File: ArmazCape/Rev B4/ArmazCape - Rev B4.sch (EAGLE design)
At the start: 167 parts, among them IC1 AT93C46EN-SH-BSOIC8, P1 RB1-125BAG1A, Q1 32.768kHz, 12.5pF, Q4 IRLML6344TRPBF, Q5 IRLML6344TRPBF, U1 L7985A, U2 L7985A, U3 DS1307ZN+, U4 24AA256-I/SN, U5 CD4050BD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

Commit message: ArmazCape - Rev B4: Reorganized schematics layout
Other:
- note added: "Mounting pads"

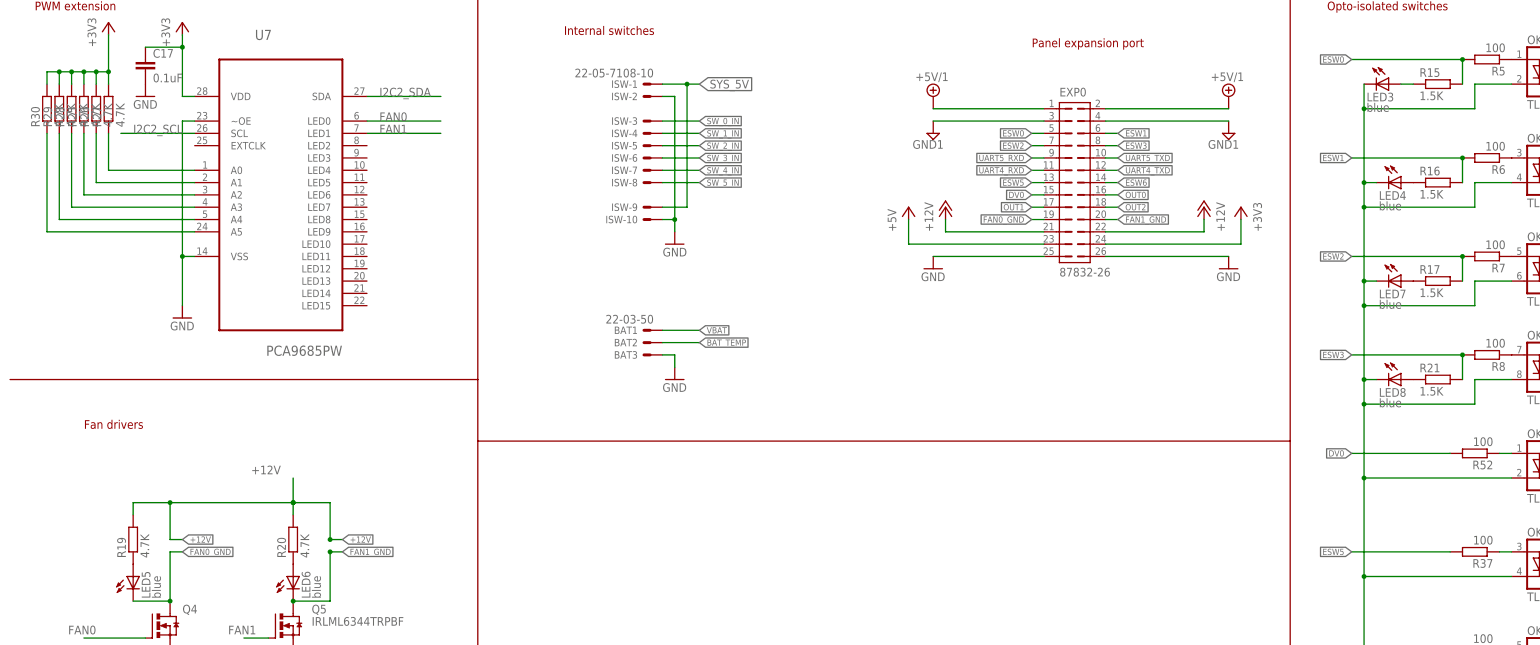
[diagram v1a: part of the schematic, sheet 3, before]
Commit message: Update attributes in ArmazCape - Rev B4
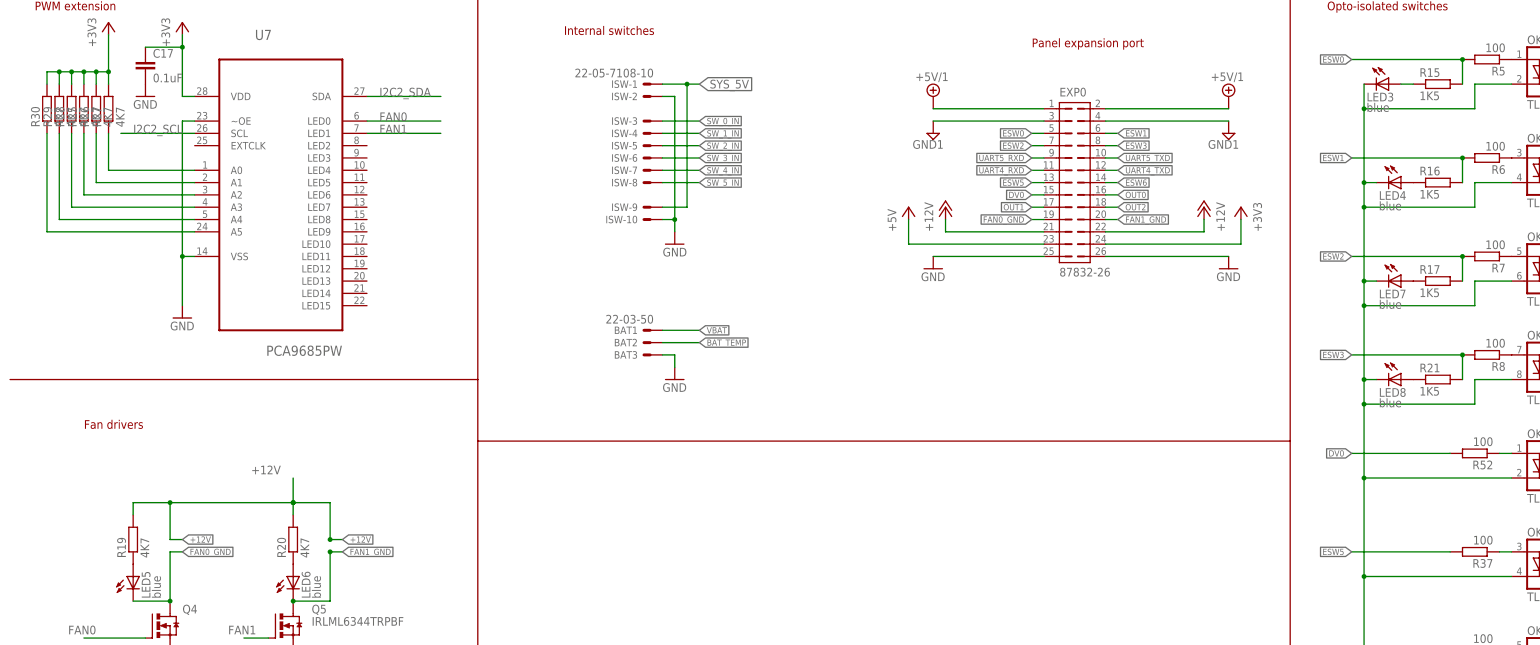
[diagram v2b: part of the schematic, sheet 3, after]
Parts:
- -25.000MHZMAAJ-T1: MF (none) -> TXC; OC_FARNELL (none) -> 1842189
- C25, C29: MPN MC0603B103K160CT -> MC0603B104K250CT; OC_FARNELL 1759003 -> 1759037
- C41: MF (none) -> MULTICOMP; MPN MC0603B104K160CT -> MC0603B104K250CT; OC_FARNELL (none) -> 1759037
- C42, C43: MF (none) -> MULTICOMP; MPN MC0603N180J500CT -> MC0603B183K160CT; OC_FARNELL (none) -> 1759006
- C9: MF MURATA -> MULTICOMP; MPN GRM1885C1H331JA01D -> MC0603B331K500CT; OC_FARNELL 8819890 -> 1759075
- GND, P1, U$7, WP: OC_FARNELL (none) -> unknown
- IC1: MF (none) -> ATMEL; OC_FARNELL (none) -> 2345627
- Q4, Q5: MF INTERNATIONAL RECTIFIER -> INFINEON
- R11: device rcl:R-EU_R0402 -> rcl:R-EU_R0603; MPN MCMR04X1600FTL -> MCWR06X1600FTL; OC_FARNELL 2072668 -> 2447260
- R13, R18, R31: value 4K7, 1% -> 4K7
- R15, R16, R17, R21: value 1.5K -> 1K5
- R19, R20, R22, R25, R26, R27, R28, R29, R30, R401, R402, R41: value 4.7K -> 4K7
- R33: MPN MCMR04X6980FTL -> MC0063W06031698R; OC_FARNELL 2073217 -> 1170773
- R68: MF (none) -> MULTICOMP; MPN MC0063W060313K01 -> MCMR06X3001FTL; OC_FARNELL (none) -> 2073461
- R73, R74: MF Multicomp Passives -> MULTICOMP; MPN MC0063W06031220R -> MCMR06X2200FTL; OC_FARNELL (none) -> 2073428
- R75: MF Multicomp Passives -> MULTICOMP; MPN MC0603WG00000T5E-TC -> MCMR06X000 PTL; OC_FARNELL (none) -> 2073345
- R76: value 4.7K -> 4K7; MF Multicomp Passives -> MULTICOMP; MPN MC0063W060314K7 -> MCMR06X4701FTL; OC_FARNELL (none) -> 2073509
- U$4: MF (none) -> MICREL SEMICONDUCTOR; MPN KSZ8851SNLI-TR -> KSZ8851SNLI TR; OC_FARNELL (none) -> 1961911

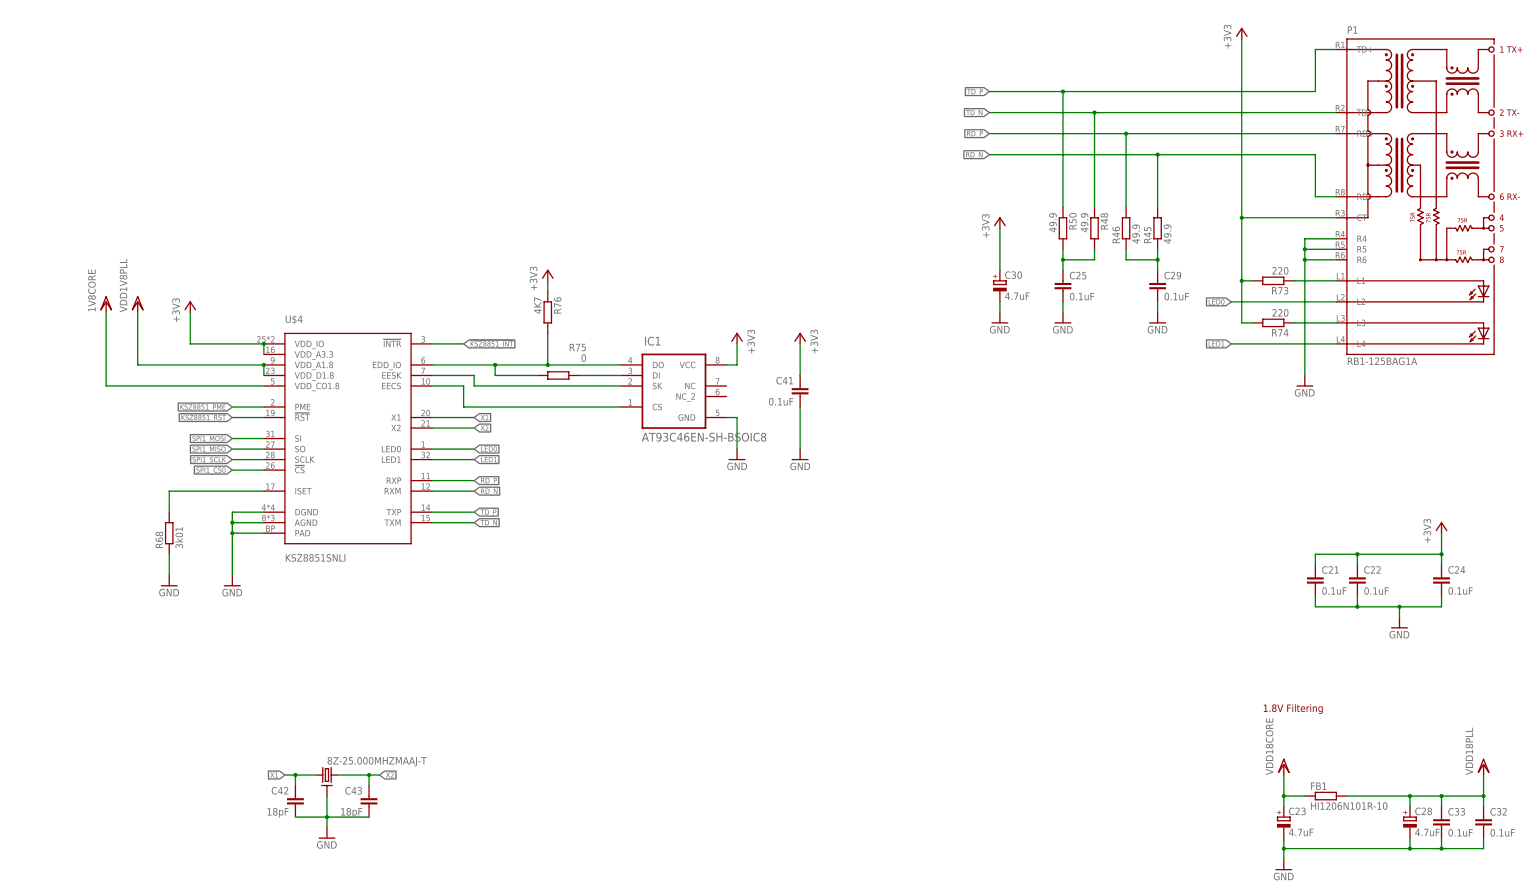
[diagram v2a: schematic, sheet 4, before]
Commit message: Reroute UART isolation
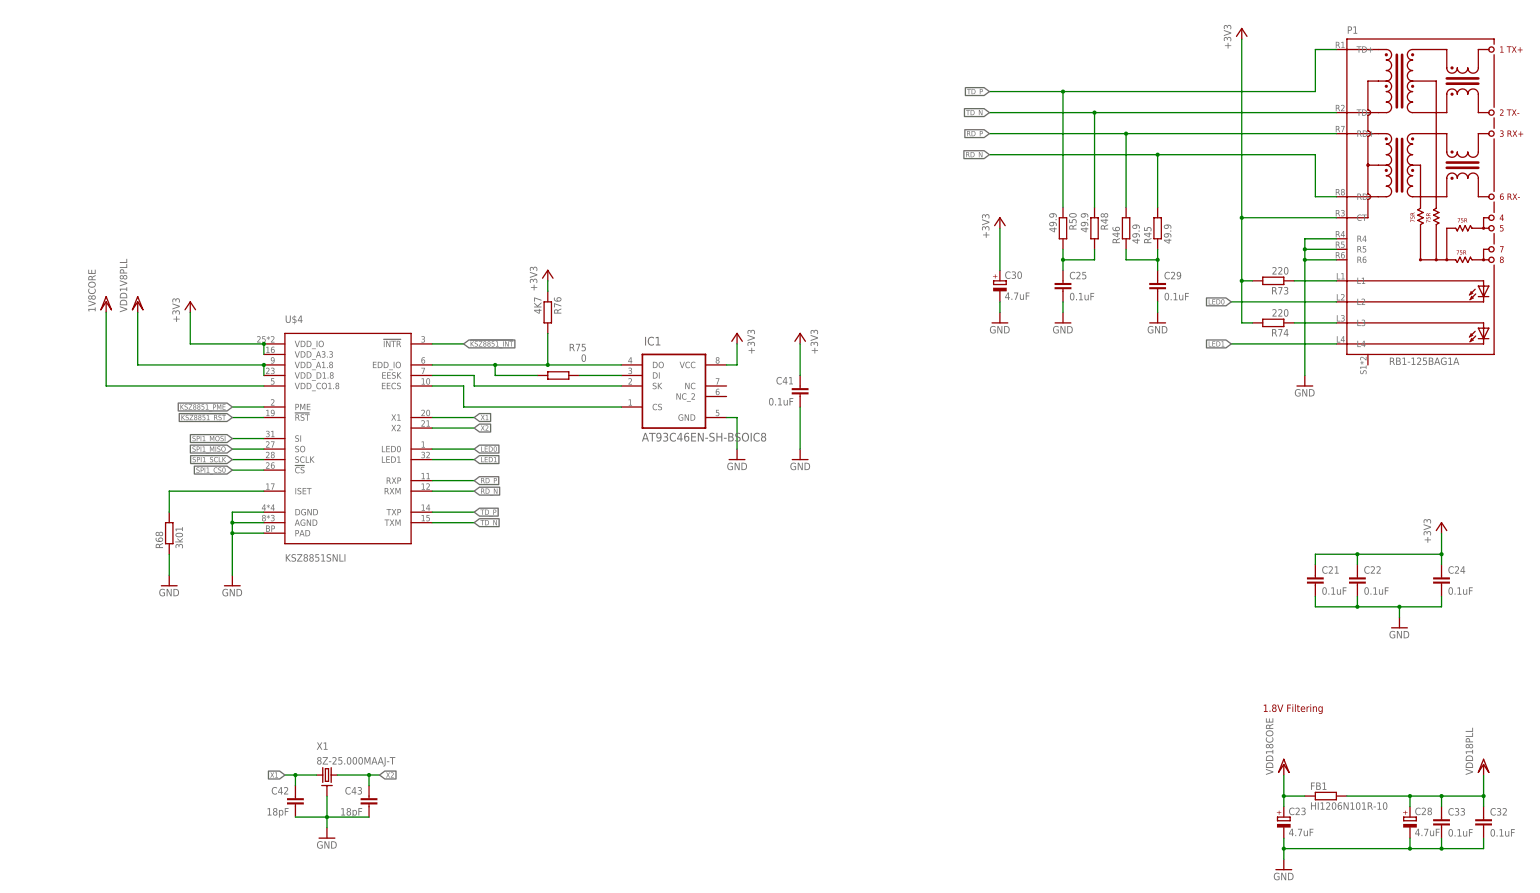
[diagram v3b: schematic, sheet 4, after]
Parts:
- X1: value 8Z-25.000MHZMAAJ-T -> 8Z-25.000MAAJ-T
- renumbered -25.000MHZMAAJ-T1 to X1
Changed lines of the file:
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@@
 <?xml version="1.0" encoding="utf-8"?>
 <!DOCTYPE eagle SYSTEM "eagle.dtd">
-<eagle version="7.6.0">
+<eagle version="7.7.0">
 <drawing>
 <settings>
@@
 <grid distance="0.1" unitdist="inch" unit="inch" style="lines" multiple="1" display="no" altdistance="0.01" altunitdist="inch" altunit="inch"/>
 <layers>
-<layer number="1" name="Top" color="16" fill="1" visible="yes" active="no"/>
-<layer number="2" name="Route2" color="17" fill="1" visible="yes" active="no"/>
-<layer number="3" name="Route3" color="4" fill="3" visible="yes" active="no"/>
-<layer number="14" name="Route14" color="1" fill="6" visible="yes" active="no"/>
-<layer number="15" name="Route15" color="19" fill="1" visible="yes" active="no"/>
-<layer number="16" name="Bottom" color="21" fill="1" visible="yes" active="no"/>
-<layer number="17" name="Pads" color="18" fill="1" visible="yes" active="no"/>
-<layer number="18" name="Vias" color="38" fill="1" visible="yes" active="no"/>
-<layer number="19" name="Unrouted" color="6" fill="1" visible="yes" active="no"/>
-<layer number="20" name="Dimension" color="7" fill="1" visible="yes" active="no"/>
-<layer number="21" name="tPlace" color="55" fill="1" visible="yes" active="no"/>
-<layer number="22" name="bPlace" color="54" fill="1" visible="yes" active="no"/>
-<layer number="23" name="tOrigins" color="15" fill="1" visible="yes" active="no"/>
-<layer number="24" name="bOrigins" color="15" fill="1" visible="yes" active="no"/>
-<layer number="25" name="tNames" color="55" fill="1" visible="yes" active="no"/>
-<layer number="26" name="bNames" color="54" fill="1" visible="yes" active="no"/>
-<layer number="27" name="tValues" color="53" fill="1" visible="yes" active="no"/>
-<layer number="28" name="bValues" color="52" fill="1" visible="yes" active="no"/>
+<layer number="1" name="Top" color="16" fill="1" visible="no" active="no"/>
+<layer number="2" name="Route2" color="17" fill="1" visible="no" active="no"/>
+<layer number="3" name="Route3" color="4" fill="3" visible="no" active="no"/>
+<layer number="14" name="Route14" color="1" fill="6" visible="no" active="no"/>
+<layer number="15" name="Route15" color="19" fill="1" visible="no" active="no"/>
+<layer number="16" name="Bottom" color="21" fill="1" visible="no" active="no"/>
+<layer number="17" name="Pads" color="18" fill="1" visible="no" active="no"/>
+<layer number="18" name="Vias" color="38" fill="1" visible="no" active="no"/>
+<layer number="19" name="Unrouted" color="6" fill="1" visible="no" active="no"/>
+<layer number="20" name="Dimension" color="7" fill="1" visible="no" active="no"/>
+<layer number="21" name="tPlace" color="55" fill="1" visible="no" active="no"/>
+<layer number="22" name="bPlace" color="54" fill="1" visible="no" active="no"/>
+<layer number="23" name="tOrigins" color="15" fill="1" visible="no" active="no"/>
+<layer number="24" name="bOrigins" color="15" fill="1" visible="no" active="no"/>
+<layer number="25" name="tNames" color="55" fill="1" visible="no" active="no"/>
+<layer number="26" name="bNames" color="54" fill="1" visible="no" active="no"/>
+<layer number="27" name="tValues" color="53" fill="1" visible="no" active="no"/>
+<layer number="28" name="bValues" color="52" fill="1" visible="no" active="no"/>
 <layer number="29" name="tStop" color="7" fill="3" visible="no" active="no"/>
 <layer number="30" name="bStop" color="7" fill="6" visible="no" active="no"/>
@@
 <layer number="35" name="tGlue" color="7" fill="4" visible="no" active="no"/>
 <layer number="36" name="bGlue" color="7" fill="5" visible="no" active="no"/>
-<layer number="37" name="tTest" color="7" fill="1" visible="yes" active="no"/>
-<layer number="38" name="bTest" color="7" fill="1" visible="yes" active="no"/>
+<layer number="37" name="tTest" color="7" fill="1" visible="no" active="no"/>
+<layer number="38" name="bTest" color="7" fill="1" visible="no" active="no"/>
 <layer number="39" name="tKeepout" color="4" fill="11" visible="no" active="no"/>
 <layer number="40" name="bKeepout" color="3" fill="11" visible="no" active="no"/>
@@
 <layer number="44" name="Drills" color="16" fill="1" visible="no" active="no"/>
 <layer number="45" name="Holes" color="35" fill="1" visible="no" active="no"/>
-<layer number="46" name="Milling" color="35" fill="1" visible="yes" active="no"/>
-<layer number="47" name="Measures" color="21" fill="1" visible="yes" active="no"/>
-<layer number="48" name="Document" color="24" fill="1" visible="yes" active="no"/>
-<layer number="49" name="Reference" color="48" fill="1" visible="yes" active="no"/>
-<layer number="50" name="dxf" color="7" fill="1" visible="yes" active="no"/>
-<layer number="51" name="tDocu" color="55" fill="1" visible="yes" active="no"/>
-<layer number="52" name="bDocu" color="54" fill="1" visible="yes" active="no"/>
-<layer number="53" name="tGND_GNDA" color="7" fill="1" visible="yes" active="no"/>
-<layer number="54" name="bGND_GNDA" color="7" fill="1" visible="yes" active="no"/>
-<layer number="56" name="wert" color="7" fill="1" visible="yes" active="no"/>
+<layer number="46" name="Milling" color="35" fill="1" visible="no" active="no"/>
+<layer number="47" name="Measures" color="21" fill="1" visible="no" active="no"/>
+<layer number="48" name="Document" color="24" fill="1" visible="no" active="no"/>
+<layer number="49" name="Reference" color="48" fill="1" visible="no" active="no"/>
+<layer number="50" name="dxf" color="7" fill="1" visible="no" active="no"/>
+<layer number="51" name="tDocu" color="55" fill="1" visible="no" active="no"/>
+<layer number="52" name="bDocu" color="54" fill="1" visible="no" active="no"/>
+<layer number="53" name="tGND_GNDA" color="7" fill="1" visible="no" active="no"/>
+<layer number="54" name="bGND_GNDA" color="7" fill="1" visible="no" active="no"/>
+<layer number="56" name="wert" color="7" fill="1" visible="no" active="no"/>
 <layer number="90" name="Modules" color="5" fill="1" visible="yes" active="yes"/>
 <layer number="91" name="Nets" color="2" fill="1" visible="yes" active="yes"/>
@@
 </part>
 <part name="+3V23" library="supply1" deviceset="+3V3" device=""/>
-<part name="-25.000MHZMAAJ-T1" library="crystal" deviceset="8Z" device="" technology="-25.000MHZMAAJ-T">
+<part name="X1" library="crystal" deviceset="8Z" device="" technology="-25.000MHZMAAJ-T" value="8Z-25.000MAAJ-T">
 <attribute name="MF" value="TXC"/>
 <attribute name="MPN" value="8Z-25.000MAAJ-T"/>
@@
 </instance>
 <instance part="+3V23" gate="G$1" x="139.7" y="190.5"/>
-<instance part="-25.000MHZMAAJ-T1" gate="G$1" x="86.36" y="68.58" smashed="yes">
-<attribute name="VALUE" x="86.36" y="71.12" size="1.778" layer="96"/>
+<instance part="X1" gate="G$1" x="86.36" y="68.58" smashed="yes">
 <attribute name="OC_NEWARK" x="86.36" y="68.58" size="1.778" layer="96" display="off"/>
 <attribute name="MF" x="86.36" y="68.58" size="1.778" layer="96" display="off"/>
 <attribute name="MPN" x="86.36" y="68.58" size="1.778" layer="96" display="off"/>
 <attribute name="OC_FARNELL" x="86.36" y="68.58" size="1.778" layer="96" display="off"/>
+<attribute name="NAME" x="83.82" y="74.676" size="1.778" layer="95"/>
+<attribute name="VALUE" x="83.82" y="71.12" size="1.778" layer="96"/>
 </instance>
 <instance part="C42" gate="G$1" x="78.74" y="63.5" rot="MR0">
@@
 </segment>
 <segment>
-<pinref part="-25.000MHZMAAJ-T1" gate="G$1" pin="2"/>
+<pinref part="X1" gate="G$1" pin="2"/>
 <pinref part="C43" gate="G$1" pin="2"/>
 <wire x1="96.52" y1="58.42" x2="86.36" y2="58.42" width="0.1524" layer="91"/>
@@
 <segment>
 <pinref part="C42" gate="G$1" pin="1"/>
-<pinref part="-25.000MHZMAAJ-T1" gate="G$1" pin="1"/>
+<pinref part="X1" gate="G$1" pin="1"/>
 <wire x1="78.74" y1="66.04" x2="78.74" y2="68.58" width="0.1524" layer="91"/>
 <wire x1="76.2" y1="68.58" x2="78.74" y2="68.58" width="0.1524" layer="91"/>
@@
 <net name="X2" class="0">
 <segment>
-<pinref part="-25.000MHZMAAJ-T1" gate="G$1" pin="3"/>
+<pinref part="X1" gate="G$1" pin="3"/>
 <pinref part="C43" gate="G$1" pin="1"/>
 <wire x1="88.9" y1="68.58" x2="96.52" y2="68.58" width="0.1524" layer="91"/>
